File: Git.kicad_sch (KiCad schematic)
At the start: 2 parts, among them U1 L7805

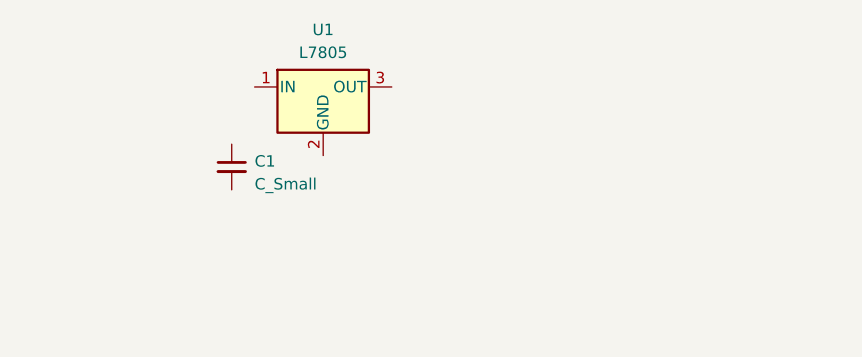
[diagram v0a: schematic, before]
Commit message: Schematic
Input and output connectors added
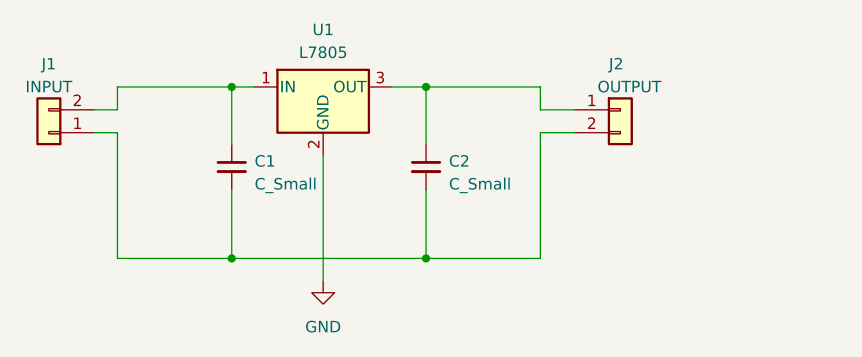
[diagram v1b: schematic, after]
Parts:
- added C2: C_Small, symbol Device:C_Small
- added J1: INPUT, symbol Connector_Generic:Conn_01x02
- added J2: OUTPUT, symbol Connector_Generic:Conn_01x02
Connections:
- net at C1.1: now also U1.1 (IN), J1.2 (Pin_2)
- net at C1.2: now also C2.2, J1.1 (Pin_1), J2.2 (Pin_2)
- net GND: now reaches U1.2 (GND)
- net at U1.3 (OUT): now also C2.1, J2.1 (Pin_1)
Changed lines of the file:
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@@
 (kicad_sch (version 20230121) (generator eeschema)
   (paper "A4")
+  (junction (at 139.7 68.58) (diameter 0) (color 0 0 0 0)
+  )
+  (junction (at 139.7 49.53) (diameter 0) (color 0 0 0 0)
+  )
+  (junction (at 161.29 68.58) (diameter 0) (color 0 0 0 0)
+  )
+  (junction (at 161.29 49.53) (diameter 0) (color 0 0 0 0)
+  )
+  (wire (pts (xy 161.29 49.53) (xy 161.29 55.88))
+    (stroke (width 0) (type default))
+  )
+  (wire (pts (xy 127 49.53) (xy 139.7 49.53))
+    (stroke (width 0) (type default))
+  )
+  (wire (pts (xy 161.29 68.58) (xy 161.29 60.96))
+    (stroke (width 0) (type default))
+  )
+  (wire (pts (xy 173.99 52.07) (xy 177.8 52.07))
+    (stroke (width 0) (type default))
+  )
+  (wire (pts (xy 127 68.58) (xy 139.7 68.58))
+    (stroke (width 0) (type default))
+  )
+  (wire (pts (xy 139.7 68.58) (xy 161.29 68.58))
+    (stroke (width 0) (type default))
+  )
+  (wire (pts (xy 139.7 60.96) (xy 139.7 68.58))
+    (stroke (width 0) (type default))
+  )
+  (wire (pts (xy 157.48 49.53) (xy 161.29 49.53))
+    (stroke (width 0) (type default))
+  )
+  (wire (pts (xy 173.99 54.61) (xy 177.8 54.61))
+    (stroke (width 0) (type default))
+  )
+  (wire (pts (xy 149.86 57.15) (xy 149.86 71.12))
+    (stroke (width 0) (type default))
+  )
+  (wire (pts (xy 124.46 52.07) (xy 127 52.07))
+    (stroke (width 0) (type default))
+  )
+  (wire (pts (xy 161.29 68.58) (xy 173.99 68.58))
+    (stroke (width 0) (type default))
+  )
+  (wire (pts (xy 161.29 49.53) (xy 173.99 49.53))
+    (stroke (width 0) (type default))
+  )
+  (wire (pts (xy 173.99 49.53) (xy 173.99 52.07))
+    (stroke (width 0) (type default))
+  )
+  (wire (pts (xy 124.46 54.61) (xy 127 54.61))
+    (stroke (width 0) (type default))
+  )
+  (wire (pts (xy 127 68.58) (xy 127 54.61))
+    (stroke (width 0) (type default))
+  )
+  (wire (pts (xy 173.99 68.58) (xy 173.99 54.61))
+    (stroke (width 0) (type default))
+  )
+  (wire (pts (xy 139.7 55.88) (xy 139.7 49.53))
+    (stroke (width 0) (type default))
+  )
+  (wire (pts (xy 127 49.53) (xy 127 52.07))
+    (stroke (width 0) (type default))
+  )
+  (wire (pts (xy 139.7 49.53) (xy 142.24 49.53))
+    (stroke (width 0) (type default))
+  )
+  (symbol (lib_id "Connector_Generic:Conn_01x02") (at 182.88 52.07 0) (unit 1)
+    (in_bom yes) (on_board yes) (dnp no)
+    (property "Reference" "J2" (at 181.61 46.99 0)
+      (effects (font (size 1.27 1.27)) (justify left))
+    )
+    (property "Value" "OUTPUT" (at 180.34 49.53 0)
+      (effects (font (size 1.27 1.27)) (justify left))
+    )
+    (property "Footprint" "" (at 182.88 52.07 0)
+      (effects (font (size 1.27 1.27)) hide)
+    )
+    (property "Datasheet" "~" (at 182.88 52.07 0)
+      (effects (font (size 1.27 1.27)) hide)
+    )
+    (pin "1")
+    (pin "2")
+    (instances
+      (project "Git"
+        (path "/1a87c68d-e2bf-43cd-a951-46dbe78c3e17"
+          (reference "J2") (unit 1)
+        )
+      )
+    )
+  )
+  (symbol (lib_id "Connector_Generic:Conn_01x02") (at 119.38 54.61 180) (unit 1)
+    (in_bom yes) (on_board yes) (dnp no) (fields_autoplaced)
+    (property "Reference" "J1" (at 119.38 46.99 0)
+      (effects (font (size 1.27 1.27)))
+    )
+    (property "Value" "INPUT" (at 119.38 49.53 0)
+      (effects (font (size 1.27 1.27)))
+    )
+    (property "Footprint" "" (at 119.38 54.61 0)
+      (effects (font (size 1.27 1.27)) hide)
+    )
+    (property "Datasheet" "~" (at 119.38 54.61 0)
+      (effects (font (size 1.27 1.27)) hide)
+    )
+    (pin "1")
+    (pin "2")
+    (instances
+      (project "Git"
+        (path "/1a87c68d-e2bf-43cd-a951-46dbe78c3e17"
+          (reference "J1") (unit 1)
+        )
+      )
+    )
+  )
+  (symbol (lib_id "Device:C_Small") (at 161.29 58.42 0) (unit 1)
+    (in_bom yes) (on_board yes) (dnp no) (fields_autoplaced)
+    (property "Reference" "C2" (at 163.83 57.7913 0)
+      (effects (font (size 1.27 1.27)) (justify left))
+    )
+    (property "Value" "C_Small" (at 163.83 60.3313 0)
+      (effects (font (size 1.27 1.27)) (justify left))
+    )
+    (property "Footprint" "" (at 161.29 58.42 0)
+      (effects (font (size 1.27 1.27)) hide)
+    )
+    (property "Datasheet" "~" (at 161.29 58.42 0)
+      (effects (font (size 1.27 1.27)) hide)
+    )
+    (pin "1")
+    (pin "2")
+    (instances
+      (project "Git"
+        (path "/1a87c68d-e2bf-43cd-a951-46dbe78c3e17"
+          (reference "C2") (unit 1)
+        )
+      )
+    )
+  )
+  (symbol (lib_id "power:GND") (at 149.86 71.12 0) (unit 1)
+    (in_bom yes) (on_board yes) (dnp no) (fields_autoplaced)
+    (property "Reference" "#PWR01" (at 149.86 77.47 0)
+      (effects (font (size 1.27 1.27)) hide)
+    )
+    (property "Value" "GND" (at 149.86 76.2 0)
+      (effects (font (size 1.27 1.27)))
+    )
+    (property "Footprint" "" (at 149.86 71.12 0)
+      (effects (font (size 1.27 1.27)) hide)
+    )
+    (property "Datasheet" "" (at 149.86 71.12 0)
+      (effects (font (size 1.27 1.27)) hide)
+    )
+    (pin "1")
+    (instances
+      (project "Git"
+        (path "/1a87c68d-e2bf-43cd-a951-46dbe78c3e17"
+          (reference "#PWR01") (unit 1)
+        )
+      )
+    )
+  )
   (symbol (lib_id "Device:C_Small") (at 139.7 58.42 0) (unit 1)
     (in_bom yes) (on_board yes) (dnp no) (fields_autoplaced)

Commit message: Power indication
Red LED added
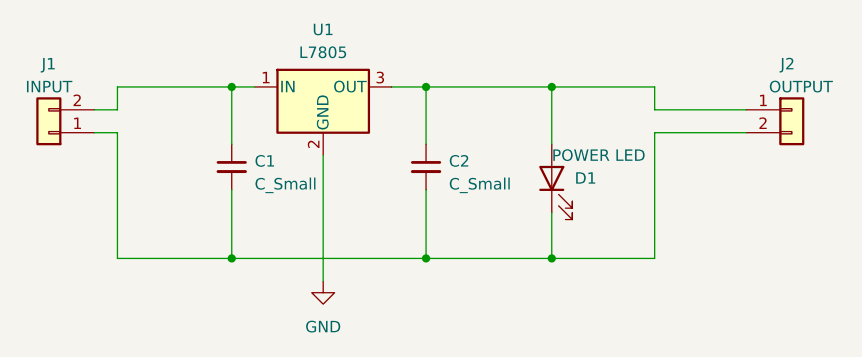
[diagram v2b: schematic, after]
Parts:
- added D1: POWER LED, symbol Device:LED
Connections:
- net at C2.1, J2.1 (Pin_1), U1.3 (OUT): now also D1.2 (A)
- net at C1.2, C2.2, J1.1 (Pin_1)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: now also D1.1 (K)
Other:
- moved on the sheet: J2
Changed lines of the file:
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@@
 (kicad_sch (version 20230121) (generator eeschema)
   (paper "A4")
+  (junction (at 175.26 49.53) (diameter 0) (color 0 0 0 0)
+  )
   (junction (at 139.7 68.58) (diameter 0) (color 0 0 0 0)
   )
   (junction (at 139.7 49.53) (diameter 0) (color 0 0 0 0)
   )
+  (junction (at 175.26 68.58) (diameter 0) (color 0 0 0 0)
+  )
   (junction (at 161.29 68.58) (diameter 0) (color 0 0 0 0)
   )
@@
     (stroke (width 0) (type default))
   )
-  (wire (pts (xy 173.99 52.07) (xy 177.8 52.07))
+  (wire (pts (xy 186.69 52.07) (xy 196.85 52.07))
     (stroke (width 0) (type default))
   )
@@
     (stroke (width 0) (type default))
   )
+  (wire (pts (xy 175.26 63.5) (xy 175.26 68.58))
+    (stroke (width 0) (type default))
+  )
   (wire (pts (xy 139.7 68.58) (xy 161.29 68.58))
     (stroke (width 0) (type default))
@@
     (stroke (width 0) (type default))
   )
-  (wire (pts (xy 173.99 54.61) (xy 177.8 54.61))
+  (wire (pts (xy 186.69 54.61) (xy 196.85 54.61))
     (stroke (width 0) (type default))
   )
@@
     (stroke (width 0) (type default))
   )
-  (wire (pts (xy 161.29 68.58) (xy 173.99 68.58))
-    (stroke (width 0) (type default))
-  )
-  (wire (pts (xy 161.29 49.53) (xy 173.99 49.53))
-    (stroke (width 0) (type default))
-  )
-  (wire (pts (xy 173.99 49.53) (xy 173.99 52.07))
+  (wire (pts (xy 161.29 68.58) (xy 175.26 68.58))
+    (stroke (width 0) (type default))
+  )
+  (wire (pts (xy 161.29 49.53) (xy 175.26 49.53))
+    (stroke (width 0) (type default))
+  )
+  (wire (pts (xy 186.69 49.53) (xy 186.69 52.07))
+    (stroke (width 0) (type default))
+  )
+  (wire (pts (xy 175.26 68.58) (xy 186.69 68.58))
+    (stroke (width 0) (type default))
+  )
+  (wire (pts (xy 175.26 49.53) (xy 175.26 55.88))
     (stroke (width 0) (type default))
   )
@@
     (stroke (width 0) (type default))
   )
+  (wire (pts (xy 175.26 49.53) (xy 186.69 49.53))
+    (stroke (width 0) (type default))
+  )
   (wire (pts (xy 127 68.58) (xy 127 54.61))
     (stroke (width 0) (type default))
   )
-  (wire (pts (xy 173.99 68.58) (xy 173.99 54.61))
+  (wire (pts (xy 186.69 68.58) (xy 186.69 54.61))
     (stroke (width 0) (type default))
   )
@@
     (stroke (width 0) (type default))
   )
-  (symbol (lib_id "Connector_Generic:Conn_01x02") (at 182.88 52.07 0) (unit 1)
+  (symbol (lib_id "Connector_Generic:Conn_01x02") (at 201.93 52.07 0) (unit 1)
     (in_bom yes) (on_board yes) (dnp no)
-    (property "Reference" "J2" (at 181.61 46.99 0)
-      (effects (font (size 1.27 1.27)) (justify left))
-    )
-    (property "Value" "OUTPUT" (at 180.34 49.53 0)
-      (effects (font (size 1.27 1.27)) (justify left))
-    )
-    (property "Footprint" "" (at 182.88 52.07 0)
-      (effects (font (size 1.27 1.27)) hide)
-    )
-    (property "Datasheet" "~" (at 182.88 52.07 0)
+    (property "Reference" "J2" (at 200.66 46.99 0)
+      (effects (font (size 1.27 1.27)) (justify left))
+    )
+    (property "Value" "OUTPUT" (at 199.39 49.53 0)
+      (effects (font (size 1.27 1.27)) (justify left))
+    )
+    (property "Footprint" "" (at 201.93 52.07 0)
+      (effects (font (size 1.27 1.27)) hide)
+    )
+    (property "Datasheet" "~" (at 201.93 52.07 0)
       (effects (font (size 1.27 1.27)) hide)
     )
@@
         )
       )
+    )
+  )
+  (symbol (lib_id "Device:LED") (at 175.26 59.69 90) (unit 1)
+    (in_bom yes) (on_board yes) (dnp no)
+    (property "Reference" "D1" (at 177.8 59.69 90)
+      (effects (font (size 1.27 1.27)) (justify right))
+    )
+    (property "Value" "POWER LED" (at 175.26 57.15 90)
+      (effects (font (size 1.27 1.27)) (justify right))
+    )
+    (property "Footprint" "" (at 175.26 59.69 0)
+      (effects (font (size 1.27 1.27)) hide)
+    )
+    (property "Datasheet" "~" (at 175.26 59.69 0)
+      (effects (font (size 1.27 1.27)) hide)
+    )
+    (pin "1")
+    (pin "2")
+    (instances
+      (project "Git"
+        (path "/1a87c68d-e2bf-43cd-a951-46dbe78c3e17"
+          (reference "D1") (unit 1)
+        )
+      )
